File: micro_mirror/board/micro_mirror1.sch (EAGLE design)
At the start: 163 parts, among them IC1 74LV7014, IC2 74LV02, IC3 74LV08, IC4 LM324D, IC5 LM324D, J1 POWER_JACKPTH_LOCK, U8 TPS62160

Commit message: in progress, changing copper spacing
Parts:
- C1: value 10nF-L -> 10nF-H
- R3: value 1M -> 10M
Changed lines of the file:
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@@
 <part name="R1" library="rcl" deviceset="R-US_" device="R1206" value="100R"/>
 <part name="R2" library="rcl" deviceset="R-US_" device="R1206" value="100R"/>
-<part name="C1" library="rcl" deviceset="C-US" device="C1206" value="10nF-L"/>
+<part name="C1" library="rcl" deviceset="C-US" device="C1206" value="10nF-H"/>
 <part name="C2" library="rcl" deviceset="C-US" device="C1206" value="10nF-L"/>
 <part name="D1" library="diode" deviceset="DIODE-" device="DO214AC" value="BYG23T-M3"/>
@@
 <part name="P+2" library="supply1" deviceset="V+" device=""/>
 <part name="GND1" library="supply1" deviceset="GND" device=""/>
-<part name="R3" library="rcl" deviceset="R-US_" device="R1206" value="1M"/>
+<part name="R3" library="rcl" deviceset="R-US_" device="R1206" value="10M"/>
 <part name="C3" library="rcl" deviceset="C-US" device="C1206" value="1nF-1k5V"/>
 <part name="R4" library="rcl" deviceset="R-US_" device="R1206" value="100k"/>

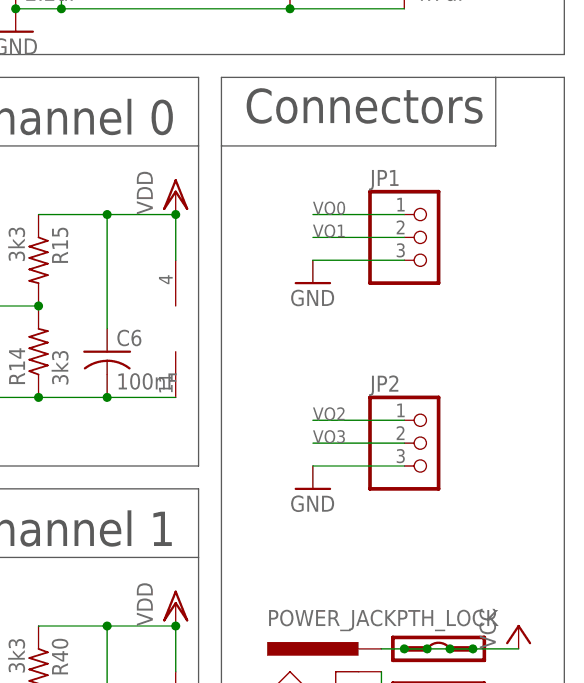
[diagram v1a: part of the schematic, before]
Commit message: bigger gap for output connectors
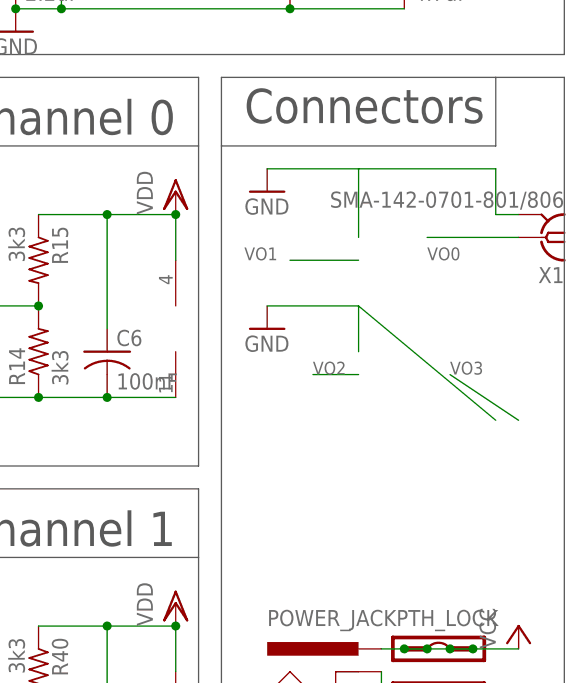
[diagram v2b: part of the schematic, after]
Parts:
- removed JP1, JP2: (no value), pinhead:PINHD-1X3
- added X1: SMA-142-0701-801/806, con-coax:SMA-142-0701-801/806
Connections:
- net GND: now also X1.2; no longer JP1.3, JP2.3
- net VO0: now also X1.1; no longer JP1.1
- net VO1: no longer JP1.2
- net VO2: no longer JP2.1
- net VO3: no longer JP2.2
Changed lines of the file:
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@@
 <?xml version="1.0" encoding="utf-8"?>
 <!DOCTYPE eagle SYSTEM "eagle.dtd">
-<eagle version="8.2.2">
+<eagle version="8.6.3">
 <drawing>
 <settings>
 <setting alwaysvectorfont="no"/>
+<setting keepoldvectorfont="yes"/>
 <setting verticaltext="up"/>
 </settings>
@@
 <part name="+3V3" library="supply1" deviceset="+3V3" device=""/>
 <part name="VDD1" library="supply1" deviceset="VDD" device=""/>
-<part name="JP1" library="pinhead" deviceset="PINHD-1X3" device=""/>
 <part name="GND5" library="supply1" deviceset="GND" device=""/>
 <part name="VDDA" library="modular_robotics" deviceset="M04" device="LOCK"/>
@@
 <part name="C31" library="rcl" deviceset="C-US" device="C1206" value="470pF"/>
 <part name="R52" library="rcl" deviceset="R-US_" device="R1206" value="1k"/>
-<part name="JP2" library="pinhead" deviceset="PINHD-1X3" device=""/>
 <part name="GND18" library="supply1" deviceset="GND" device=""/>
 <part name="U$15" library="modular_robotics" deviceset="HGTD1N120BNS" device=""/>
@@
 </part>
 <part name="GND15" library="supply1" deviceset="GND" device=""/>
+<part name="X1" library="con-coax" library_urn="urn:adsk.eagle:library:133" deviceset="SMA-" device="142-0701-801/806" package3d_urn="urn:adsk.eagle:package:6214/1"/>
 </parts>
 <sheets>
@@
 <instance part="+3V3" gate="G$1" x="114.3" y="114.3"/>
 <instance part="VDD1" gate="G$1" x="302.26" y="116.84"/>
-<instance part="JP1" gate="A" x="330.2" y="111.76"/>
-<instance part="GND5" gate="1" x="317.5" y="106.68"/>
+<instance part="GND5" gate="1" x="312.42" y="116.84"/>
 <instance part="VDDA" gate="G$1" x="266.7" y="154.94" rot="R90"/>
 <instance part="R16" gate="G$1" x="261.62" y="101.6"/>
@@
 <instance part="C31" gate="G$1" x="48.26" y="7.62"/>
 <instance part="R52" gate="G$1" x="43.18" y="10.16"/>
-<instance part="JP2" gate="A" x="330.2" y="88.9"/>
-<instance part="GND18" gate="1" x="317.5" y="83.82"/>
+<instance part="GND18" gate="1" x="312.42" y="101.6"/>
 <instance part="U$15" gate="G$1" x="160.02" y="-25.4"/>
 <instance part="U$16" gate="G$1" x="160.02" y="-40.64"/>
@@
 </instance>
 <instance part="GND15" gate="1" x="48.26" y="0"/>
+<instance part="X1" gate="G1" x="342.9" y="111.76" rot="R180"/>
 </instances>
 <busses>
@@
 </segment>
 <segment>
-<pinref part="JP1" gate="A" pin="3"/>
-<wire x1="327.66" y1="109.22" x2="317.5" y2="109.22" width="0.1524" layer="91"/>
 <pinref part="GND5" gate="1" pin="GND"/>
+<wire x1="312.42" y1="119.38" x2="322.58" y2="119.38" width="0.1524" layer="91"/>
+<wire x1="322.58" y1="119.38" x2="337.82" y2="119.38" width="0.1524" layer="91"/>
+<wire x1="337.82" y1="119.38" x2="337.82" y2="114.3" width="0.1524" layer="91"/>
+<wire x1="322.58" y1="111.76" x2="322.58" y2="119.38" width="0.1524" layer="91"/>
+<pinref part="X1" gate="G1" pin="2"/>
+<wire x1="340.36" y1="114.3" x2="337.82" y2="114.3" width="0.1524" layer="91"/>
 </segment>
 <segment>
@@
 </segment>
 <segment>
-<pinref part="JP2" gate="A" pin="3"/>
 <pinref part="GND18" gate="1" pin="GND"/>
-<wire x1="317.5" y1="86.36" x2="327.66" y2="86.36" width="0.1524" layer="91"/>
+<wire x1="312.42" y1="104.14" x2="322.58" y2="104.14" width="0.1524" layer="91"/>
+<wire x1="322.58" y1="99.06" x2="322.58" y2="104.14" width="0.1524" layer="91"/>
+<wire x1="322.58" y1="104.14" x2="337.82" y2="91.44" width="0.1524" layer="91"/>
 </segment>
 <segment>
@@
 </segment>
 <segment>
-<pinref part="JP1" gate="A" pin="1"/>
-<wire x1="327.66" y1="114.3" x2="317.5" y2="114.3" width="0.1524" layer="91"/>
-<label x="317.5" y="114.3" size="1.4224" layer="95"/>
+<wire x1="340.36" y1="111.76" x2="330.2" y2="111.76" width="0.1524" layer="91"/>
+<label x="330.2" y="109.22" size="1.4224" layer="95"/>
+<pinref part="X1" gate="G1" pin="1"/>
 </segment>
 </net>
@@
 <net name="VO1" class="0">
 <segment>
-<pinref part="JP1" gate="A" pin="2"/>
-<wire x1="327.66" y1="111.76" x2="317.5" y2="111.76" width="0.1524" layer="91"/>
-<label x="317.5" y="111.76" size="1.4224" layer="95"/>
-</segment>
-<segment>
 <pinref part="R30" gate="G$1" pin="2"/>
 <pinref part="R33" gate="G$1" pin="2"/>
@@
 <junction x="195.58" y="66.04"/>
 <label x="193.04" y="73.66" size="1.4224" layer="95"/>
+</segment>
+<segment>
+<wire x1="322.58" y1="109.22" x2="314.96" y2="109.22" width="0.1524" layer="91"/>
+<label x="309.88" y="109.22" size="1.4224" layer="95"/>
 </segment>
 </net>
@@
 </segment>
 <segment>
-<pinref part="JP2" gate="A" pin="1"/>
-<wire x1="327.66" y1="91.44" x2="317.5" y2="91.44" width="0.1524" layer="91"/>
-<label x="317.5" y="91.44" size="1.4224" layer="95"/>
+<label x="317.5" y="96.52" size="1.4224" layer="95"/>
+<wire x1="317.5" y1="96.52" x2="322.58" y2="96.52" width="0.1524" layer="91"/>
 </segment>
 </net>
@@
 <net name="VO3" class="0">
 <segment>
-<pinref part="JP2" gate="A" pin="2"/>
-<wire x1="327.66" y1="88.9" x2="317.5" y2="88.9" width="0.1524" layer="91"/>
-<label x="317.5" y="88.9" size="1.4224" layer="95"/>
+<label x="332.74" y="96.52" size="1.4224" layer="95"/>
+<wire x1="340.36" y1="91.44" x2="332.74" y2="96.52" width="0.1524" layer="91"/>
 </segment>
 <segment>
@@
 </schematic>
 </drawing>
+<compatibility>
+<note version="8.2" severity="warning">
+Since Version 8.2, EAGLE supports online libraries. The ids
+of those online libraries will not be understood (or retained)
+with this version.
+</note>
+<note version="8.3" severity="warning">
+Since Version 8.3, EAGLE supports URNs for individual library
+assets (packages, symbols, and devices). The URNs of those assets
+will not be understood (or retained) with this version.
+</note>
+<note version="8.3" severity="warning">
+Since Version 8.3, EAGLE supports the association of 3D packages
+with devices in libraries, schematics, and board files. Those 3D
+packages will not be understood (or retained) with this version.
+</note>
+</compatibility>
 </eagle>

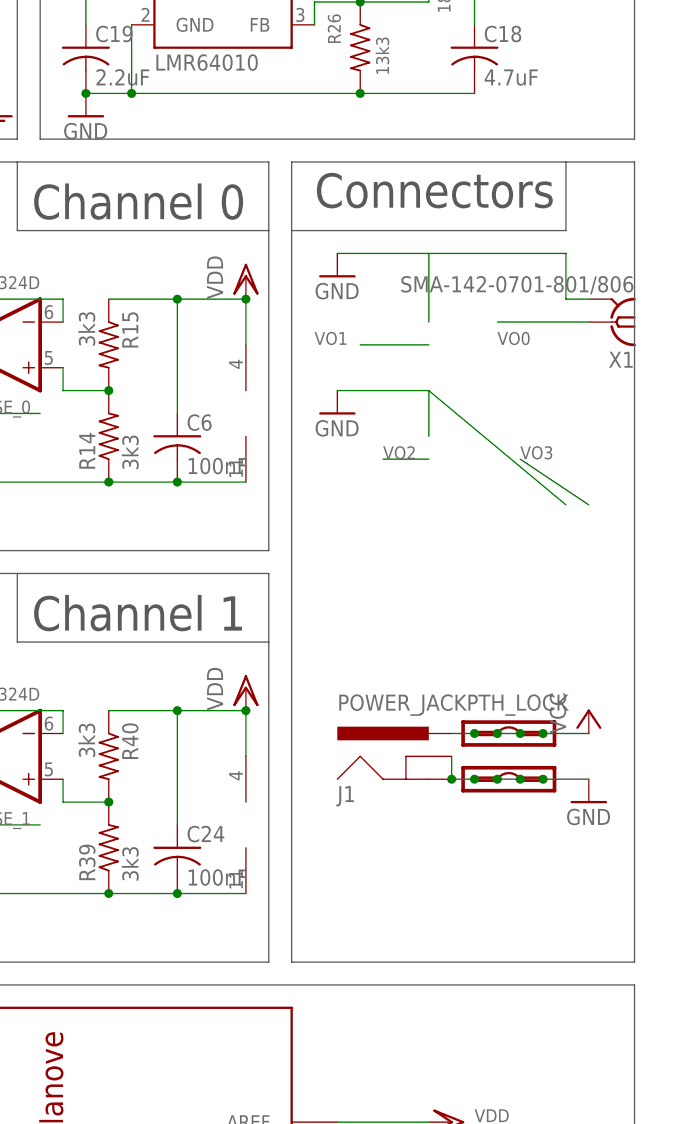
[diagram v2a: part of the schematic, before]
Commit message: making gap > 40 mil to handle 1kV.
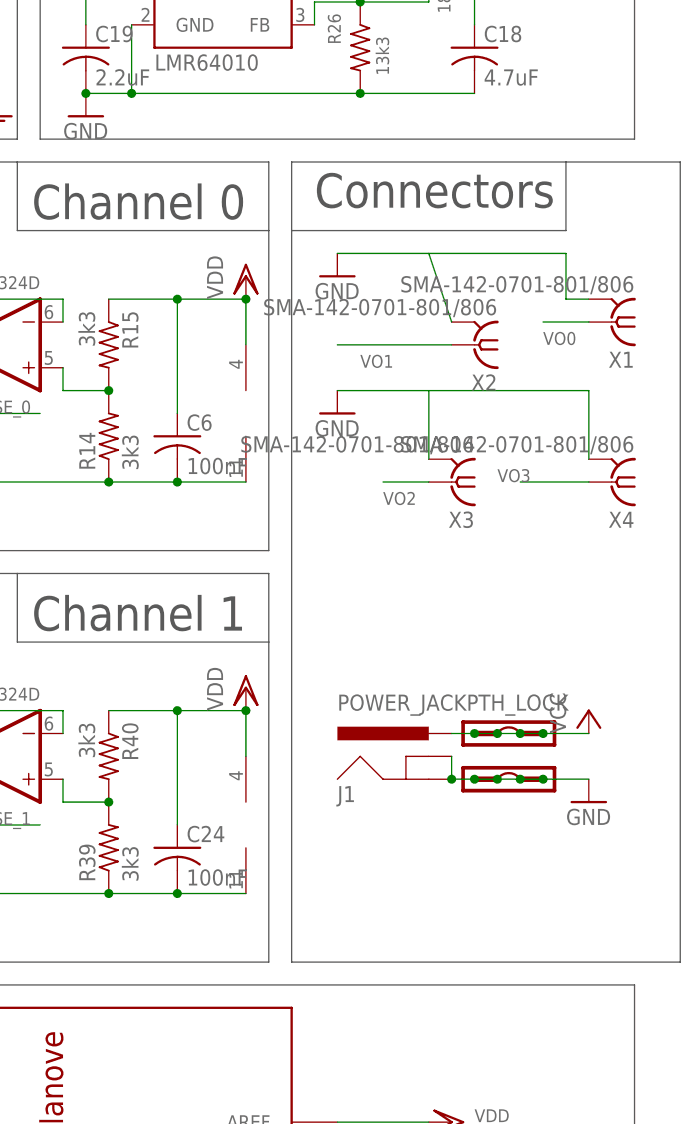
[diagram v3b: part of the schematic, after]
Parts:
- added X2, X3, X4: SMA-142-0701-801/806, con-coax:SMA-142-0701-801/806
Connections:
- net GND: now also X2.2, X3.2, X4.2
- net VO1: now also X2.1
- net VO2: now also X3.1
- net VO3: now also X4.1
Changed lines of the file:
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@@
 <part name="GND15" library="supply1" deviceset="GND" device=""/>
 <part name="X1" library="con-coax" library_urn="urn:adsk.eagle:library:133" deviceset="SMA-" device="142-0701-801/806" package3d_urn="urn:adsk.eagle:package:6214/1"/>
+<part name="X2" library="con-coax" library_urn="urn:adsk.eagle:library:133" deviceset="SMA-" device="142-0701-801/806" package3d_urn="urn:adsk.eagle:package:6214/1"/>
+<part name="X3" library="con-coax" library_urn="urn:adsk.eagle:library:133" deviceset="SMA-" device="142-0701-801/806" package3d_urn="urn:adsk.eagle:package:6214/1"/>
+<part name="X4" library="con-coax" library_urn="urn:adsk.eagle:library:133" deviceset="SMA-" device="142-0701-801/806" package3d_urn="urn:adsk.eagle:package:6214/1"/>
 </parts>
 <sheets>
@@
 <instance part="GND15" gate="1" x="48.26" y="0"/>
 <instance part="X1" gate="G1" x="342.9" y="111.76" rot="R180"/>
+<instance part="X2" gate="G1" x="327.66" y="109.22" rot="R180"/>
+<instance part="X3" gate="G1" x="325.12" y="93.98" rot="R180"/>
+<instance part="X4" gate="G1" x="342.9" y="93.98" rot="R180"/>
 </instances>
 <busses>
@@
 <wire x1="307.34" y1="121.92" x2="307.34" y2="129.54" width="0.762" layer="92"/>
 <wire x1="307.34" y1="129.54" x2="337.82" y2="129.54" width="0.762" layer="92"/>
-<wire x1="337.82" y1="129.54" x2="345.44" y2="129.54" width="0.762" layer="92"/>
-<wire x1="345.44" y1="129.54" x2="345.44" y2="40.64" width="0.762" layer="92"/>
-<wire x1="345.44" y1="40.64" x2="307.34" y2="40.64" width="0.762" layer="92"/>
+<wire x1="337.82" y1="129.54" x2="350.52" y2="129.54" width="0.762" layer="92"/>
+<wire x1="350.52" y1="129.54" x2="350.52" y2="40.64" width="0.762" layer="92"/>
+<wire x1="350.52" y1="40.64" x2="307.34" y2="40.64" width="0.762" layer="92"/>
 <wire x1="307.34" y1="121.92" x2="337.82" y2="121.92" width="0.762" layer="92"/>
 <wire x1="337.82" y1="121.92" x2="337.82" y2="129.54" width="0.762" layer="92"/>
@@
 <wire x1="322.58" y1="119.38" x2="337.82" y2="119.38" width="0.1524" layer="91"/>
 <wire x1="337.82" y1="119.38" x2="337.82" y2="114.3" width="0.1524" layer="91"/>
-<wire x1="322.58" y1="111.76" x2="322.58" y2="119.38" width="0.1524" layer="91"/>
+<wire x1="325.12" y1="111.76" x2="322.58" y2="119.38" width="0.1524" layer="91"/>
 <pinref part="X1" gate="G1" pin="2"/>
 <wire x1="340.36" y1="114.3" x2="337.82" y2="114.3" width="0.1524" layer="91"/>
+<pinref part="X2" gate="G1" pin="2"/>
 </segment>
 <segment>
@@
 <pinref part="GND18" gate="1" pin="GND"/>
 <wire x1="312.42" y1="104.14" x2="322.58" y2="104.14" width="0.1524" layer="91"/>
-<wire x1="322.58" y1="99.06" x2="322.58" y2="104.14" width="0.1524" layer="91"/>
-<wire x1="322.58" y1="104.14" x2="337.82" y2="91.44" width="0.1524" layer="91"/>
+<wire x1="322.58" y1="96.52" x2="322.58" y2="104.14" width="0.1524" layer="91"/>
+<wire x1="322.58" y1="104.14" x2="340.36" y2="104.14" width="0.1524" layer="91"/>
+<wire x1="340.36" y1="104.14" x2="340.36" y2="96.52" width="0.1524" layer="91"/>
+<pinref part="X3" gate="G1" pin="2"/>
+<pinref part="X4" gate="G1" pin="2"/>
 </segment>
 <segment>
@@
 </segment>
 <segment>
-<wire x1="340.36" y1="111.76" x2="330.2" y2="111.76" width="0.1524" layer="91"/>
-<label x="330.2" y="109.22" size="1.4224" layer="95"/>
+<wire x1="340.36" y1="111.76" x2="335.28" y2="111.76" width="0.1524" layer="91"/>
+<label x="335.28" y="109.22" size="1.4224" layer="95"/>
 <pinref part="X1" gate="G1" pin="1"/>
 </segment>
@@
 </segment>
 <segment>
-<wire x1="322.58" y1="109.22" x2="314.96" y2="109.22" width="0.1524" layer="91"/>
-<label x="309.88" y="109.22" size="1.4224" layer="95"/>
+<wire x1="325.12" y1="109.22" x2="312.42" y2="109.22" width="0.1524" layer="91"/>
+<label x="314.96" y="106.68" size="1.4224" layer="95"/>
+<pinref part="X2" gate="G1" pin="1"/>
 </segment>
 </net>
@@
 </segment>
 <segment>
-<label x="317.5" y="96.52" size="1.4224" layer="95"/>
-<wire x1="317.5" y1="96.52" x2="322.58" y2="96.52" width="0.1524" layer="91"/>
+<label x="317.5" y="91.44" size="1.4224" layer="95"/>
+<wire x1="317.5" y1="93.98" x2="322.58" y2="93.98" width="0.1524" layer="91"/>
+<pinref part="X3" gate="G1" pin="1"/>
 </segment>
 </net>
@@
 <net name="VO3" class="0">
 <segment>
-<label x="332.74" y="96.52" size="1.4224" layer="95"/>
-<wire x1="340.36" y1="91.44" x2="332.74" y2="96.52" width="0.1524" layer="91"/>
-</segment>
-<segment>
+<label x="330.2" y="93.98" size="1.4224" layer="95"/>
+<wire x1="340.36" y1="93.98" x2="332.74" y2="93.98" width="0.1524" layer="91"/>
+<pinref part="X4" gate="G1" pin="1"/>
+</segment>
+<segment>
